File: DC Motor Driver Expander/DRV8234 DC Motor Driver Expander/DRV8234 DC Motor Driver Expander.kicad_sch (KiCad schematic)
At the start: 20 parts, among them IC1 DRV8234RTER, J1 POWER, J2 CNTRL_IN, J3 CNTRL_OUT, J4 I2C, J5 MOTOR

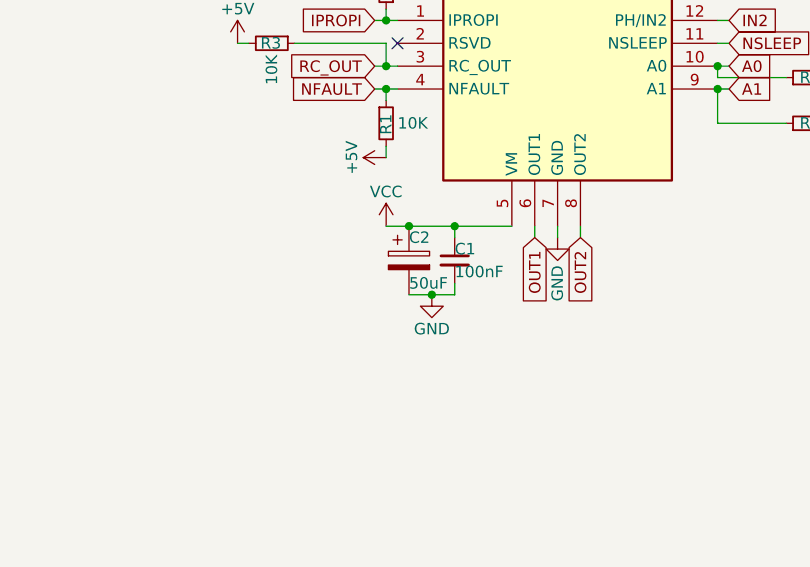
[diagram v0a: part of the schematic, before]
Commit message: Update
BOM Added
50uF -> 100uF Capacitor
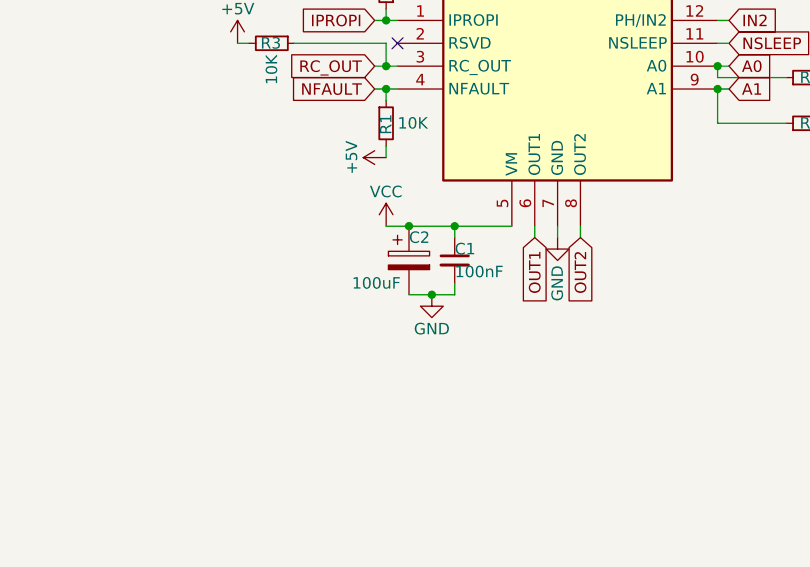
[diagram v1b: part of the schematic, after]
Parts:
- C2: value 50uF -> 100uF; footprint Capacitor_SMD:C_Elec_5x5.8 -> Capacitor_SMD:C_Elec_8x10.2
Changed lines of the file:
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@@
       (effects (font (size 1.27 1.27)) (justify left))
     )
-    (property "Value" "50uF" (at 78.74 83.82 0)
+    (property "Value" "100uF" (at 72.39 83.82 0)
       (effects (font (size 1.27 1.27)) (justify left))
     )
-    (property "Footprint" "Capacitor_SMD:C_Elec_5x5.8" (at 79.7052 85.09 0)
+    (property "Footprint" "Capacitor_SMD:C_Elec_8x10.2" (at 79.7052 85.09 0)
       (effects (font (size 1.27 1.27)) hide)
     )
